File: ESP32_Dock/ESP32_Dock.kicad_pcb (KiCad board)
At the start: 2 copper layers, 52.8 x 29.5 mm, 7 parts, among them J1 Conn_01x04, J2 Conn_01x04, J3 Conn_01x04, J4 Conn_01x07, J5 Conn_01x13

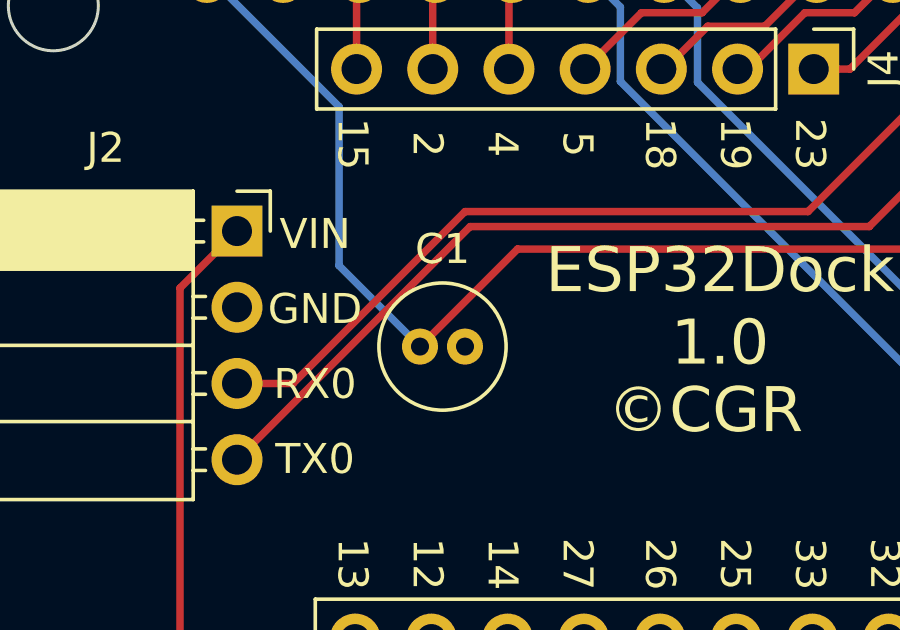
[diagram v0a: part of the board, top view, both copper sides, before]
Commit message: Fixed capacitor size on ESP32 dock
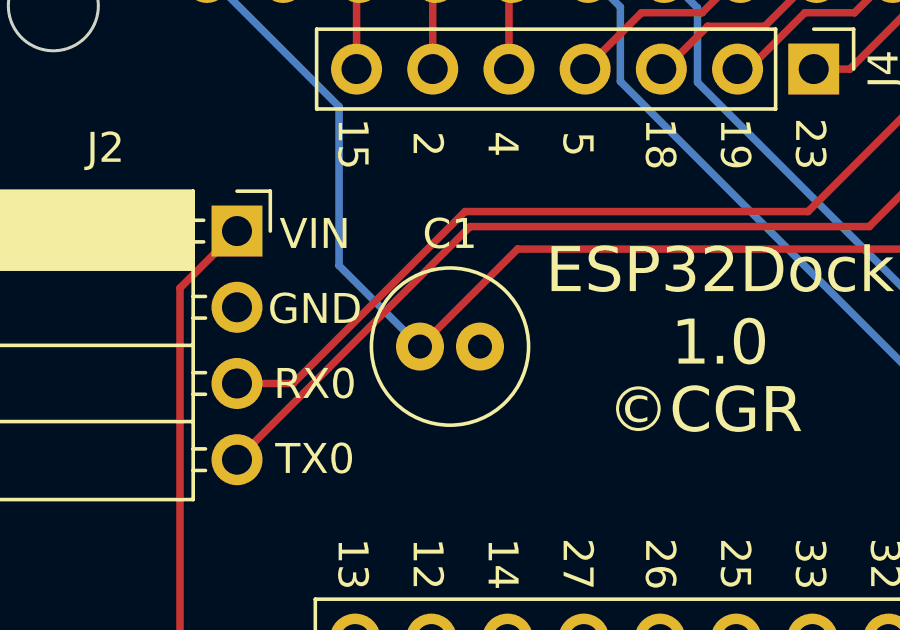
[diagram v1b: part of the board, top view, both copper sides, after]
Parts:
- C1: value 100uF -> 22uF; footprint Capacitor_THT:C_Radial_D4.0mm_H5.0mm_P1.50mm -> Capacitor_THT:C_Radial_D5.0mm_H11.0mm_P2.00mm
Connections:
- J3 pad 1: /VCC -> /VIN
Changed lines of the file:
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@@
       (stroke (width 0.1) (type solid)) (layer "F.Fab"))
     (pad "1" thru_hole rect (at 0 0) (size 1.7 1.7) (drill 1) (layers "*.Cu" "*.Mask")
-      (net 1 "/VCC") (pinfunction "Pin_1") (pintype "passive"))
+      (net 5 "/VIN") (pinfunction "Pin_1") (pintype "passive"))
     (pad "2" thru_hole oval (at 0 2.54) (size 1.7 1.7) (drill 1) (layers "*.Cu" "*.Mask")
       (net 2 "/GND") (pinfunction "Pin_2") (pintype "passive"))
@@
     )
   )
-  (footprint "Capacitor_THT:C_Radial_D4.0mm_H5.0mm_P1.50mm" (layer "F.Cu")
+  (footprint "Capacitor_THT:C_Radial_D5.0mm_H11.0mm_P2.00mm" (layer "F.Cu")
     (at 75 46.75)
-    (descr "C, Radial series, Radial, pin pitch=1.50mm, diameter=4mm, height=5mm, Non-Polar Electrolytic Capacitor")
-    (tags "C Radial series Radial pin pitch 1.50mm diameter 4mm height 5mm Non-Polar Electrolytic Capacitor")
+    (descr "C, Radial series, Radial, pin pitch=2.00mm, diameter=5mm, height=11mm, Non-Polar Electrolytic Capacitor")
+    (tags "C Radial series Radial pin pitch 2.00mm diameter 5mm height 11mm Non-Polar Electrolytic Capacitor")
     (property "Sheetfile" "ESP32_Dock.kicad_sch")
     (property "Sheetname" "")
@@
     (property "ki_keywords" "cap capacitor")
     (attr through_hole)
-    (fp_text reference "C1" (at 0.75 -3.25) (layer "F.SilkS")
-        (effects (font (size 1 1) (thickness 0.15)))
-    )
-    (fp_text value "100uF" (at 0.75 3.25) (layer "F.Fab")
-        (effects (font (size 1 1) (thickness 0.15)))
-    )
-    (fp_text user "${REFERENCE}" (at 0.75 0) (layer "F.Fab")
-        (effects (font (size 0.8 0.8) (thickness 0.12)))
-    )
-    (fp_circle (center 0.75 0) (end 2.87 0)
+    (fp_text reference "C1" (at 1 -3.75) (layer "F.SilkS")
+        (effects (font (size 1 1) (thickness 0.15)))
+    )
+    (fp_text value "22uF" (at 1 3.75) (layer "F.Fab")
+        (effects (font (size 1 1) (thickness 0.15)))
+    )
+    (fp_text user "${REFERENCE}" (at 1 0) (layer "F.Fab")
+        (effects (font (size 1 1) (thickness 0.15)))
+    )
+    (fp_circle (center 1 0) (end 3.62 0)
       (stroke (width 0.12) (type solid)) (fill none) (layer "F.SilkS"))
-    (fp_circle (center 0.75 0) (end 3 0)
+    (fp_circle (center 1 0) (end 3.75 0)
       (stroke (width 0.05) (type solid)) (fill none) (layer "F.CrtYd"))
-    (fp_circle (center 0.75 0) (end 2.75 0)
+    (fp_circle (center 1 0) (end 3.5 0)
       (stroke (width 0.1) (type solid)) (fill none) (layer "F.Fab"))
-    (pad "1" thru_hole circle (at 0 0) (size 1.2 1.2) (drill 0.6) (layers "*.Cu" "*.Mask")
+    (pad "1" thru_hole circle (at 0 0) (size 1.6 1.6) (drill 0.8) (layers "*.Cu" "*.Mask")
       (net 1 "/VCC") (pintype "passive"))
-    (pad "2" thru_hole circle (at 1.5 0) (size 1.2 1.2) (drill 0.6) (layers "*.Cu" "*.Mask")
+    (pad "2" thru_hole circle (at 2 0) (size 1.6 1.6) (drill 0.8) (layers "*.Cu" "*.Mask")
       (net 2 "/GND") (pintype "passive"))
-    (model "${KICAD6_3DMODEL_DIR}/Capacitor_THT.3dshapes/C_Radial_D4.0mm_H5.0mm_P1.50mm.wrl"
-      (offset (xyz 0 0 0))
-      (scale (xyz 1 1 1))
+    (model "${KICAD6_3DMODEL_DIR}/Capacitor_THT.3dshapes/C_Radial_D5.0mm_H11.0mm_P2.00mm.wrl"
+      (offset (xyz 0 0 0))
+      (scale (xyz 1 1 1))

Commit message: Final fabrication checks
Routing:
- net /VIN: track 18.0 -> 55.0 mm, vias 0 -> 2
- net /VCC: track 43.7 -> 37.9 mm
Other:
- board text added: "+"
